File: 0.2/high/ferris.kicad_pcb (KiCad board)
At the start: 2 copper layers, 219.1 x 95.2 mm, 106 parts, among them J1 USB C, K0_0 KEYSW, K0_1 KEYSW, K0_2 KEYSW, K0_3 KEYSW, K0_4 KEYSW, K0_5 KEYSW, K0_6 KEYSW, K0_7 KEYSW, K0_8 KEYSW, K0_9 KEYSW, K1_0 KEYSW, K1_1 KEYSW, K1_2 KEYSW, K1_3 KEYSW, K1_4 KEYSW, K1_5 KEYSW, K1_6 KEYSW, K1_7 KEYSW, K1_8 KEYSW, K1_9 KEYSW, K2_0 KEYSW, K2_1 KEYSW, K2_2 KEYSW, K2_3 KEYSW, K2_4 KEYSW, K2_5 KEYSW, K2_6 KEYSW, K2_7 KEYSW, K2_8 KEYSW, K2_9 KEYSW, K3_3 KEYSW, K3_4 KEYSW, K3_5 KEYSW, K3_6 KEYSW, Q1 DTC123J, SW1 SW_PUSH, U1 STM32F072CBTx, U2 MCP23017_SO, U3 MCP1700-3302E_SOT23, U4 SRV05-4

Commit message: Remove last few references to ferris.pretty and the entire directory
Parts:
- added REF**: mouse-bite-2mm-slot-with-space-for-track, panelization:mouse-bite-2mm-slot-with-space-for-track, F.Cu at (124.0, 81.7)
- added REF**: mouse-bite-2mm-slot-with-space-for-track, panelization:mouse-bite-2mm-slot-with-space-for-track, F.Cu at (110.5, 41.4)
- added REF**: mouse-bite-2mm-slot-with-space-for-track, panelization:mouse-bite-2mm-slot-with-space-for-track, F.Cu at (137.6, 41.6)
- G*** (x2): footprint ferris:tall_ferris_copper_pad -> copper_pads:ferris_high
- G***: footprint ferris:safe_rust -> silkscreens:safe_rust
- G***: footprint ferris:unsafe_rust -> silkscreens:unsafe_rust
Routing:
- net i2c_sda_right: track 27.5 -> 26.8 mm

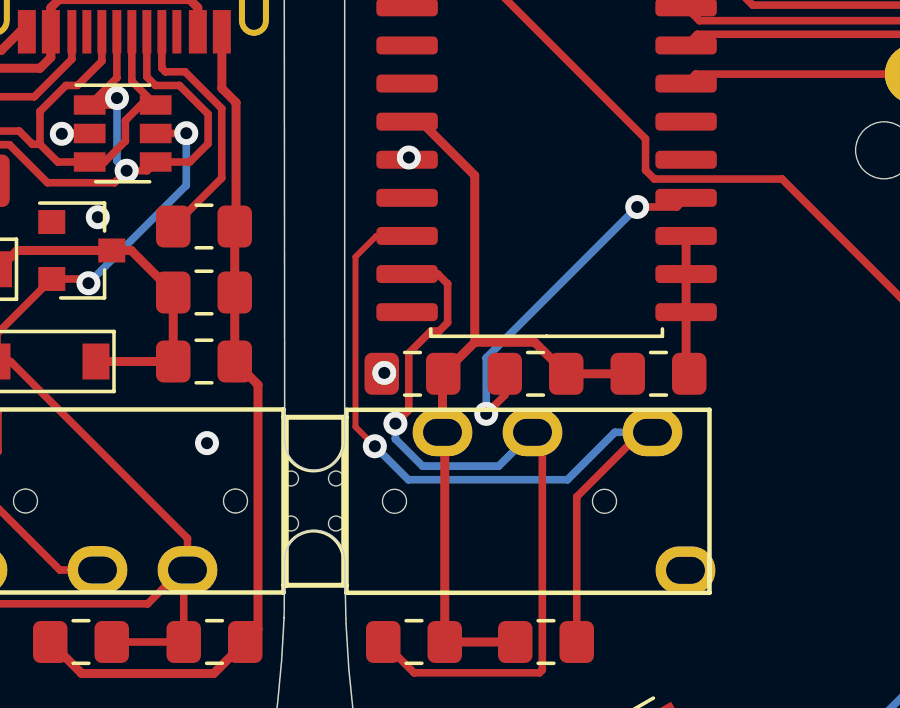
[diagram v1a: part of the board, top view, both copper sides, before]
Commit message: Fix unconnected pads in 0.2/high caught by DRC
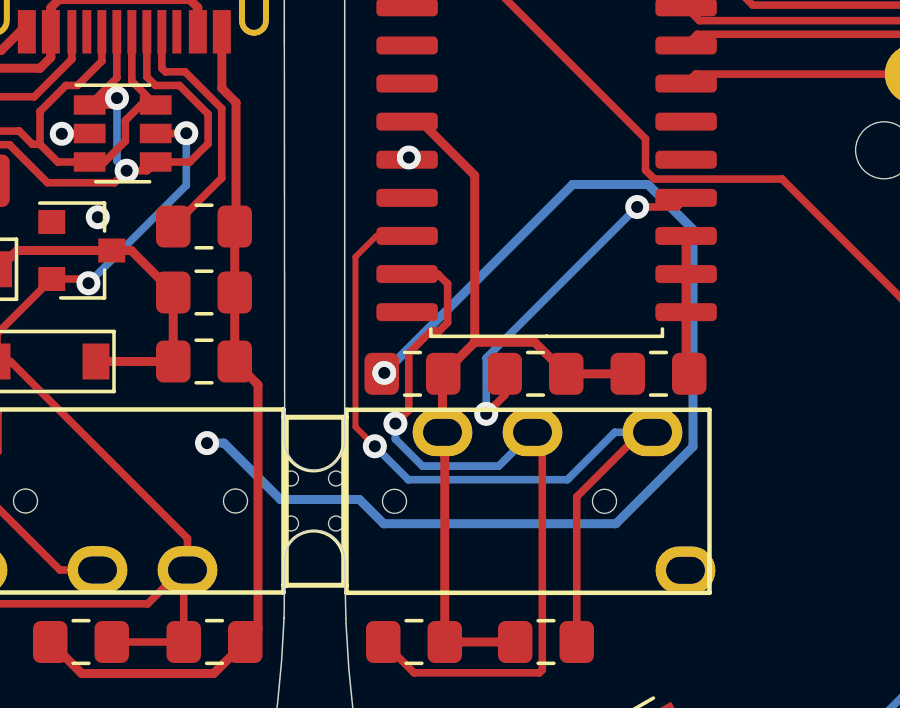
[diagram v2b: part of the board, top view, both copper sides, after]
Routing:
- net GND: track 164.7 -> 203.8 mm

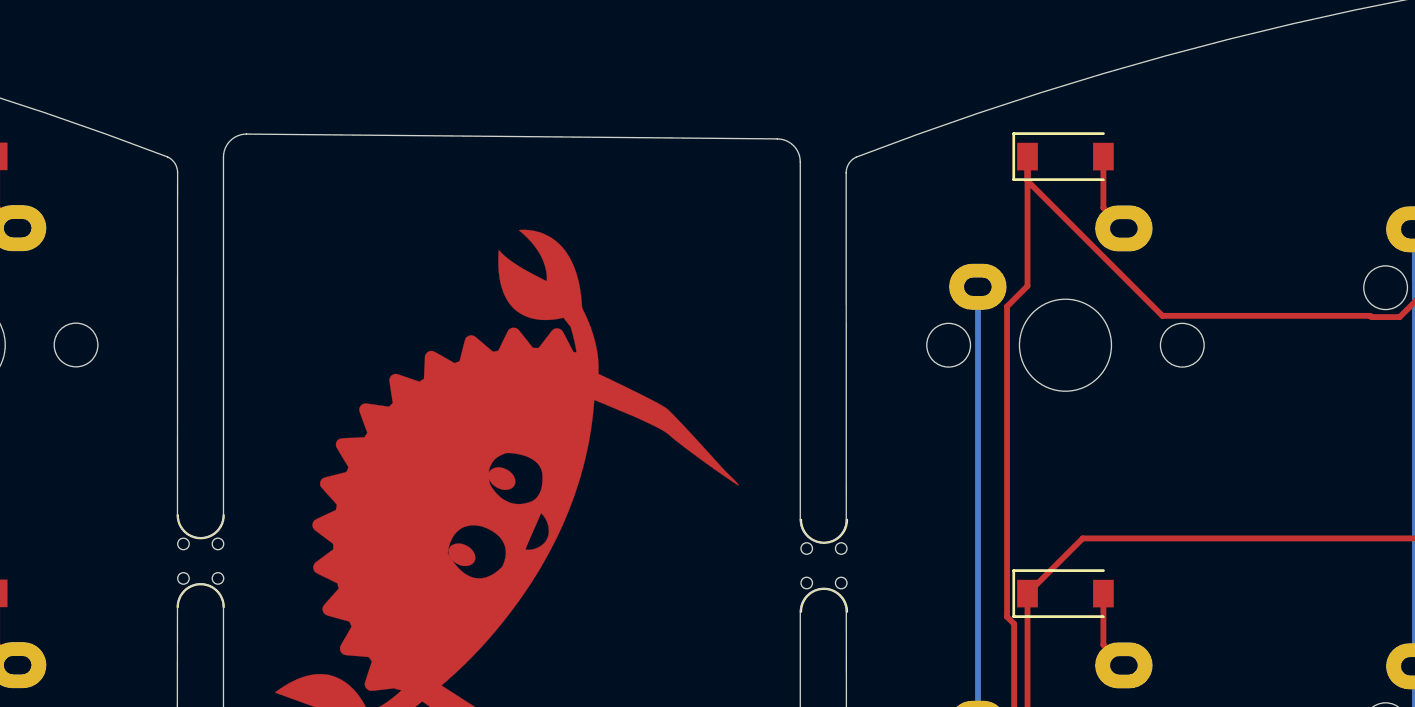
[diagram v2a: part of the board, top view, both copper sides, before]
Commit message: 0.2/high: Fix missing ground fills area that my automated renders helped me spot
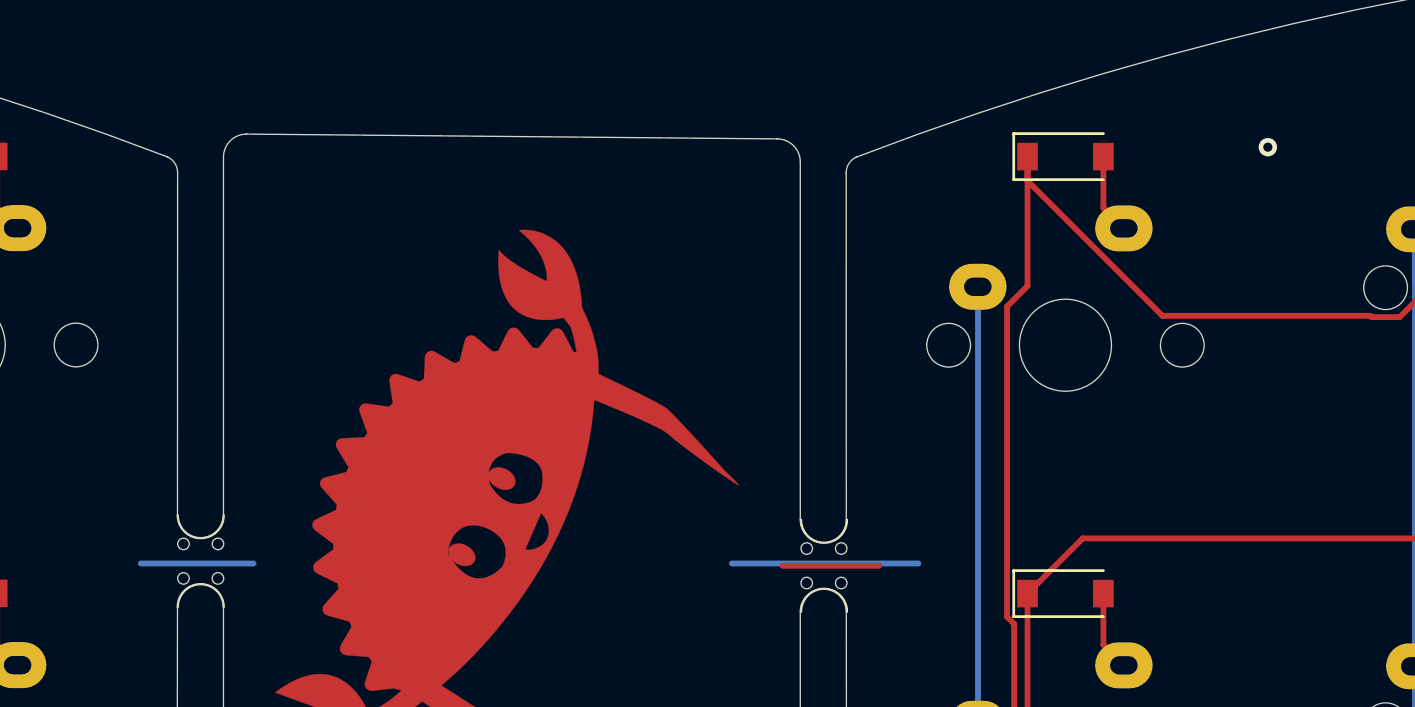
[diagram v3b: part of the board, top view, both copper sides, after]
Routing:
- net GND: track 203.8 -> 221.0 mm, vias 12 -> 13

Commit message: 0.2/high: Add human readable "Part Name" field
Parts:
- C12, C13: value 0.1u -> 0.1uF
- D0_0, D0_1, D0_2, D0_3, D0_4, D0_5, D0_6, D0_7, D0_8, D0_9, D1_0, D1_1, D1_2, D1_3, D1_4, D1_5, D1_6, D1_7, D1_8, D1_9, D2_0, D2_1, D2_2, D2_3, D2_4, D2_5, D2_6, D2_7, D2_8, D2_9, D3, D3_3, D3_4, D3_5, D3_6: value D -> 1N4148W
- J1: value USB C -> TYPE-C-31-M-12
- Jack0, Jack1: value TRRS -> PJ-320A
- Q1: value DTC123J -> PDTC123JT,215
- R1, R2: value 5.1K -> 5.1kΩ
- R3, R4, R5: value 100k -> 100kΩ
- R6: value 10k -> 10kΩ
- R7, R8: value 4.7k -> 4.7kΩ
- SW1: value SW_PUSH -> B3U-1000P
- U1: value STM32F072CBTx -> STM32F072CBT6
- U2: value MCP23017_SO -> MCP23017-E/SO
- U3: value MCP1700-3302E_SOT23 -> MCP1700T-3302E/TT
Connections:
- J1 pad A8: (no net) -> Net-(J1-PadA8)
- J1 pad B8: (no net) -> Net-(J1-PadB8)
- U2 pad 11: (no net) -> Net-(U2-Pad11)
- U2 pad 14: (no net) -> Net-(U2-Pad14)
- U2 pad 19: (no net) -> Net-(U2-Pad19)
- U2 pad 20: (no net) -> Net-(U2-Pad20)
- U2 pad 26: (no net) -> Net-(U2-Pad26)
- U2 pad 27: (no net) -> Net-(U2-Pad27)
- U2 pad 28: (no net) -> Net-(U2-Pad28)
- U2 pad 5: (no net) -> Net-(U2-Pad5)
- U2 pad 6: (no net) -> Net-(U2-Pad6)
- U2 pad 7: (no net) -> Net-(U2-Pad7)
- U2 pad 8: (no net) -> Net-(U2-Pad8)
